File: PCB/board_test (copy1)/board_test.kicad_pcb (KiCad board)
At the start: 4 copper layers, 160 parts, among them J1 USB_A, J10 Conn_01x02_Female, J11 Conn_01x03_Male, J12 Conn_01x03_Male, J13 Conn_01x03_Male, J14 Conn_01x03_Male, J15 Conn_01x02_Female, J2 Conn_02x06_Top_Bottom, J3 Conn_02x06_Top_Bottom, J4 Conn_02x06_Top_Bottom, J5 Conn_02x06_Top_Bottom, J6 Conn_02x06_Top_Bottom, J7 Conn_02x06_Top_Bottom, J9 Conn_01x02_Female, U1 TMUX1119, U10 LTC2245, U11 RenzoChip, U2 TMUX1119, U3 LT1763, U4 LT1763, U5 NCP164ASN180T1G, U6 LTC1983-3, U7 LTC1983-3, U8 NCP164ASN180T1G, U9 SN74AUC2G06

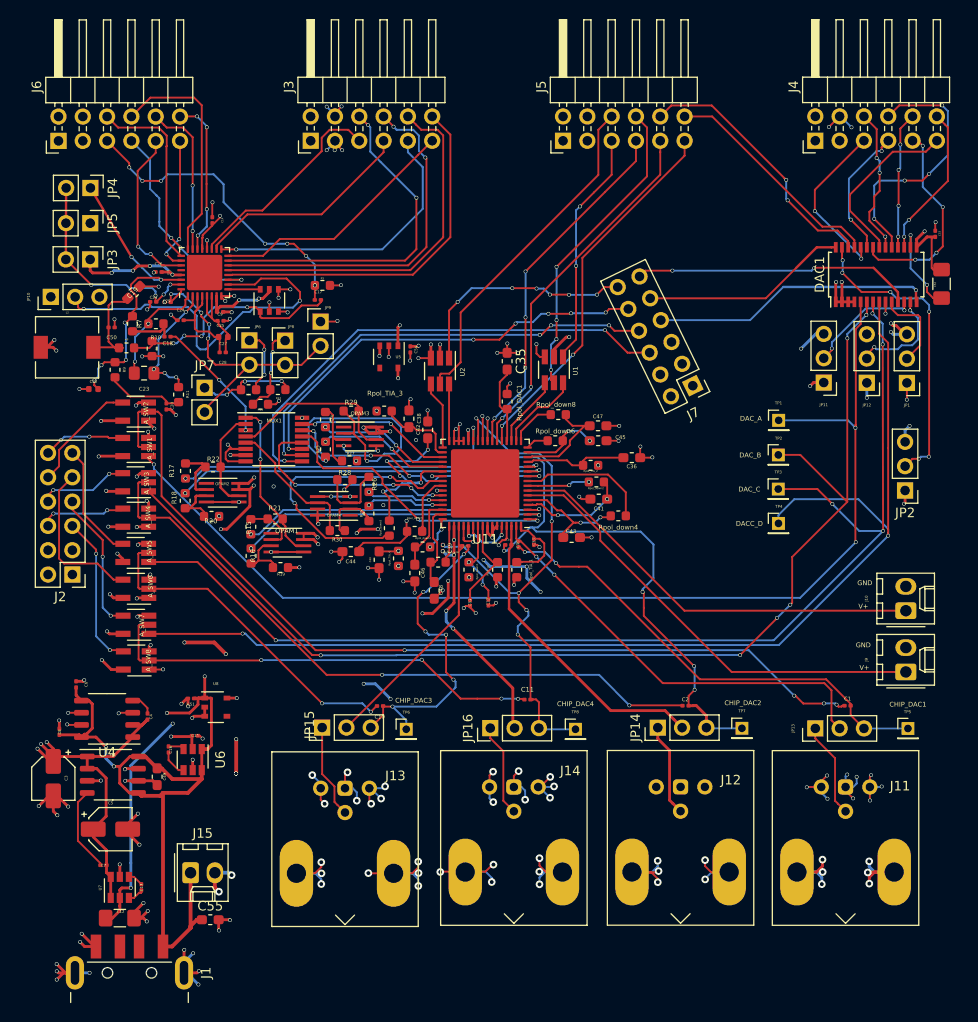
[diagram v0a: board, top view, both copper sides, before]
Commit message: Vivado project added
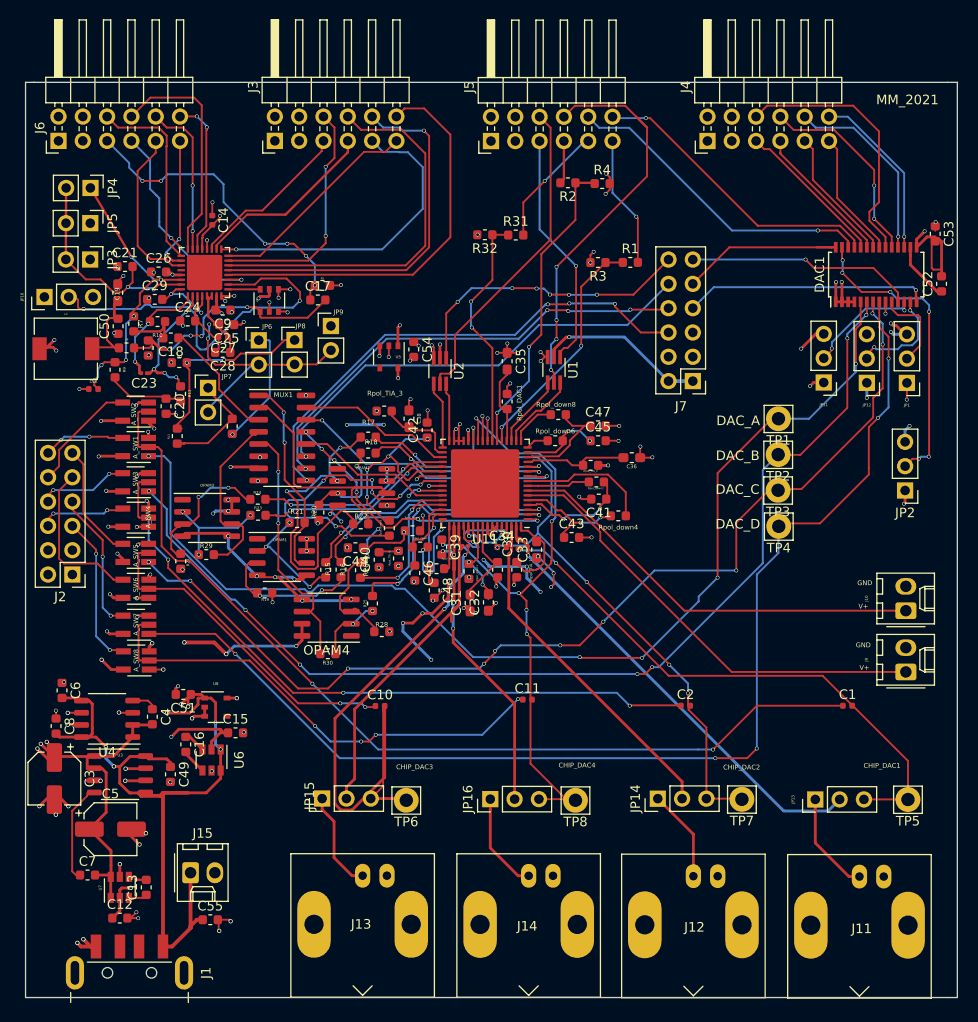
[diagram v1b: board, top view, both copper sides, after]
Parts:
- added R1: R_US, Resistor_SMD:R_0603_1608Metric, F.Cu at (220.9, 36.3)
- added R2: R_US, Resistor_SMD:R_0603_1608Metric, F.Cu at (214.3, 28.0)
- added R3: R_US, Resistor_SMD:R_0603_1608Metric, F.Cu at (217.5, 36.4)
- added R31: R_US, Resistor_SMD:R_0603_1608Metric, F.Cu at (208.9, 33.5)
- added R32: R_US, Resistor_SMD:R_0603_1608Metric, F.Cu at (205.7, 33.5)
- added R4: R_US, Resistor_SMD:R_0603_1608Metric, F.Cu at (217.9, 28.1)
- C1, C10, C11, C14, C2, C30, C34: footprint Capacitor_SMD:C_0201_0603Metric -> Capacitor_SMD:C_0402_1005Metric
- C12, C52: footprint Capacitor_SMD:C_1206_3216Metric_Pad1.42x1.75mm_HandSolder -> Capacitor_SMD:C_0603_1608Metric
- C13, C15, C16, C17, C18, C20, C21, C24, C25, C26, C28, C29, C39, C50, C51, C53, C54, C6, C7, C8, C9: footprint Capacitor_SMD:C_0201_0603Metric -> Capacitor_SMD:C_0603_1608Metric
- C23: footprint Capacitor_SMD:C_0805_2012Metric_Pad1.15x1.40mm_HandSolder -> Capacitor_SMD:C_0201_0603Metric
- C3, C5: footprint Capacitor_SMD:CP_Elec_4x3 -> Capacitor_SMD:CP_Elec_5x3.9
- C31, C32, C33: footprint Capacitor_SMD:C_0201_0603Metric -> Capacitor_SMD:C_0603_1608Metric_Pad1.05x0.95mm_HandSolder
- C4: value 1uF -> 0.01uF; footprint Capacitor_SMD:C_0201_0603Metric -> Capacitor_SMD:C_0603_1608Metric
- C40, C41, C42, C43, C44, C45, C46, C47, C48, C49, C55: footprint Capacitor_SMD:C_0603_1608Metric_Pad1.05x0.95mm_HandSolder -> Capacitor_SMD:C_0603_1608Metric
- J11, J12, J13, J14: value Conn_01x03_Male -> Conn_01x02_Male; footprint Connector_Coaxial:BNC_Win_364A2x95_Horizontal -> Connector_Coaxial:BNC_Amphenol_B6252HB-NPP3G-50_Horizontal
- MUX1: footprint Package_SO:TSSOP-16_4.4x5mm_P0.65mm -> Package_SO:SOIC-16_3.9x9.9mm_P1.27mm
- OPAM1, OPAM2, OPAM3, OPAM4: footprint Package_SO:SSOP-8_2.95x2.8mm_P0.65mm -> Package_SO:SO-8_3.9x4.9mm_P1.27mm
- TP1, TP2, TP3, TP4, TP5, TP6, TP7, TP8: footprint Connector_PinHeader_2.00mm:PinHeader_1x01_P2.00mm_Vertical -> Connector_Pin:Pin_D1.4mm_L8.5mm_W2.8mm_FlatFork
- U1, U2: footprint Package_TO_SOT_SMD:SOT-23-6_Handsoldering -> Package_TO_SOT_SMD:SOT-363_SC-70-6_Handsoldering
- moved R29 21.3 mm to (176.6, 66.9)
- moved R27 20.5 mm to (173.9, 67.6), turned to 90 degrees
- moved R18 19.8 mm to (193.5, 56.3), turned to 0 degrees
- moved R17 19.4 mm to (193.5, 54.6), turned to 180 degrees
- moved OPAM3 18.1 mm to (176.6, 63.0)
- moved R22 16.5 mm to (192.7, 63.7)
- moved R28 16.3 mm to (194.9, 74.9)
- moved OPAM2 14.6 mm to (192.8, 59.8)
- moved R30 12.9 mm to (189.3, 77.2)
- moved OPAM4 11.7 mm to (189.1, 73.5)
- moved R13 11.6 mm to (173.5, 54.5), turned to 90 degrees
- moved J4 11.3 mm to (228.9, 23.6)
- moved R20 11.2 mm to (188.3, 62.5), turned to 90 degrees
- moved R24 10.9 mm to (181.9, 61.1), turned to 0 degrees
- moved R23 9.86 mm to (182.0, 62.8), turned to 180 degrees
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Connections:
- J11 pad 1: GND -> Detector1
- J11 pad 2: Detector1 -> GND
- J12 pad 1: GND -> Detector2
- J12 pad 2: Detector2 -> GND
- J13 pad 1: GND -> Detector3
- J13 pad 2: Detector3 -> GND
- J14 pad 1: GND -> Detector4
- J14 pad 2: Detector4 -> GND
- U11 pad 21: JB7:Y18 -> chip_clk18
- U11 pad 22: JB8:Y19 -> chip_rst18
- U11 pad 23: JB9:W18 -> chip_data_in18
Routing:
- net GND: track 287.7 -> 124.7 mm, vias 170 -> 110
- net +5V: track 197.3 -> 121.3 mm, vias 5 -> 8
- net JB9:W18: track 37.6 -> 4.51 mm, vias 4 -> 0
- net chip_rst18: track 0.00 -> 32.4 mm, vias 0 -> 2
- net VIN_TIA_3_EXT: track 53.3 -> 80.7 mm, vias 7 -> 3
- net Net-(OPAM2-Pad2): track 6.38 -> 33.4 mm, vias 0 -> 3
- net +3V3: track 142.3 -> 115.4 mm, vias 40 -> 31
- net -3V3: track 123.8 -> 97.4 mm, vias 8 -> 12
- net JB8:Y19: track 38.4 -> 12.8 mm, vias 2 -> 1
- net JB7:Y18: track 39.3 -> 13.8 mm, vias 2 -> 1
- net chip_data_in18: track 0.00 -> 25.1 mm, vias 0 -> 2
- net chip_clk18: track 0.00 -> 25.0 mm, vias 0 -> 2
- net VCC_FPGA: track 71.4 -> 91.3 mm
- net VOUT_int_2-: track 39.3 -> 19.7 mm
- net VOUT_int_2+: track 38.3 -> 19.7 mm
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- removed copper zone on In1.Cu, net GND_FPGA
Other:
- board outline added: 97.4 x 95.6 mm
- board text added: "DAC_D"
- board text added: "MM_2021"
- board text removed: "DACC_D"
